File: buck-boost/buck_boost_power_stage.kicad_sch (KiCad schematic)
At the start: 21 parts, among them K1 Relay_SPDT, K2 Relay_SPDT, Q1 Q_NMOS_GDS, Q2 Q_NMOS_GDS, Q3 Q_NMOS_GDS, Q4 Q_NMOS_GDS, Q5 Q_NMOS_GDS

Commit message: Updating schematics notes
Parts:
- removed C15, C17: TBD, symbol Device:C_Polarized
- C14, C16: footprint (none) -> CL_Capacitor_PTH:C_Rect_L43.0mm_W36.0mm_P37.50_27.50_22.50mm_S20.3_10.2mm_Film
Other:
- note added: "Notes [1] V_s1 and V_s3 are the source voltages of Q1 and Q3. These nodes are used as reference for their gate drivers. [2] Two of these are bulk electrolytic capacitors, and one is low-esr (lower capacitance) capacitors."
- note removed: "Ceramic or film caps?"
- note removed: "Notes [1] V_s1 and V_s3 are the source voltages of Q1 and Q3. These nodes are used as reference for their gate drivers. [2] Two of these are bulk electrolytic capacitors, and two are low-esr (lower capacitance) capacitors."
- moved on the sheet: C14, C8, C9, K1, K2, Q5, R6

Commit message: Working on gate drivers of buck boost platform
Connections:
- net S1 renamed G_S1
- net S2 renamed G_S2
- net S3 renamed G_S3
- net S4 renamed G_S4
- net S_load renamed G_Sload
- net V_s1 renamed Vs_S1
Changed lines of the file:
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@@
 		)
 	)
-	(label "S_load"
+	(label "G_Sload"
 		(at 229.87 52.07 180)
 		(fields_autoplaced yes)
@@
 		)
 	)
-	(label "V_s3"
+	(label "Vs_S3"
 		(at 67.31 83.82 0)
 		(fields_autoplaced yes)
@@
 		)
 	)
-	(label "S1"
+	(label "G_S1"
 		(at 67.31 76.2 0)
 		(fields_autoplaced yes)
@@
 		)
 	)
-	(label "S2"
+	(label "G_S2"
 		(at 92.71 76.2 0)
 		(fields_autoplaced yes)
@@
 		)
 	)
-	(label "S1"
+	(label "G_S1"
 		(at 105.41 36.83 180)
 		(fields_autoplaced yes)
@@
 		)
 	)
-	(label "V_s1"
+	(label "Vs_S1"
 		(at 67.31 78.74 0)
 		(fields_autoplaced yes)
@@
 		)
 	)
-	(label "V_s3"
+	(label "Vs_S3"
 		(at 143.51 44.45 0)
 		(fields_autoplaced yes)
@@
 		)
 	)
-	(label "S3"
+	(label "G_S3"
 		(at 67.31 81.28 0)
 		(fields_autoplaced yes)
@@
 		)
 	)
-	(label "S3"
+	(label "G_S3"
 		(at 151.13 36.83 0)
 		(fields_autoplaced yes)
@@
 		)
 	)
-	(label "V_s1"
+	(label "Vs_S1"
 		(at 113.03 44.45 180)
 		(fields_autoplaced yes)
@@
 		)
 	)
-	(label "S4"
+	(label "G_S4"
 		(at 151.13 52.07 0)
 		(fields_autoplaced yes)
@@
 		)
 	)
-	(label "S_load"
+	(label "G_Sload"
 		(at 92.71 81.28 0)
 		(fields_autoplaced yes)
@@
 		)
 	)
-	(label "S4"
+	(label "G_S4"
 		(at 92.71 78.74 0)
 		(fields_autoplaced yes)
@@
 		)
 	)
-	(label "S2"
+	(label "G_S2"
 		(at 105.41 52.07 180)
 		(fields_autoplaced yes)
@@
 		)
 	)
-	(hierarchical_label "V_s3"
+	(hierarchical_label "Vs_S3"
 		(shape bidirectional)
 		(at 73.66 83.82 0)
@@
 		)
 	)
-	(hierarchical_label "S4"
+	(hierarchical_label "G_S4"
 		(shape bidirectional)
 		(at 101.6 78.74 0)
@@
 		)
 	)
-	(hierarchical_label "V_s1"
+	(hierarchical_label "Vs_S1"
 		(shape bidirectional)
 		(at 73.66 78.74 0)
@@
 		)
 	)
-	(hierarchical_label "S3"
+	(hierarchical_label "G_S3"
 		(shape bidirectional)
 		(at 73.66 81.28 0)
@@
 		)
 	)
-	(hierarchical_label "S1"
+	(hierarchical_label "G_S1"
 		(shape bidirectional)
 		(at 73.66 76.2 0)
@@
 		)
 	)
-	(hierarchical_label "S2"
+	(hierarchical_label "G_S2"
 		(shape bidirectional)
 		(at 101.6 76.2 0)
@@
 		)
 	)
-	(hierarchical_label "S_load"
+	(hierarchical_label "G_Sload"
 		(shape bidirectional)
 		(at 101.6 81.28 0)

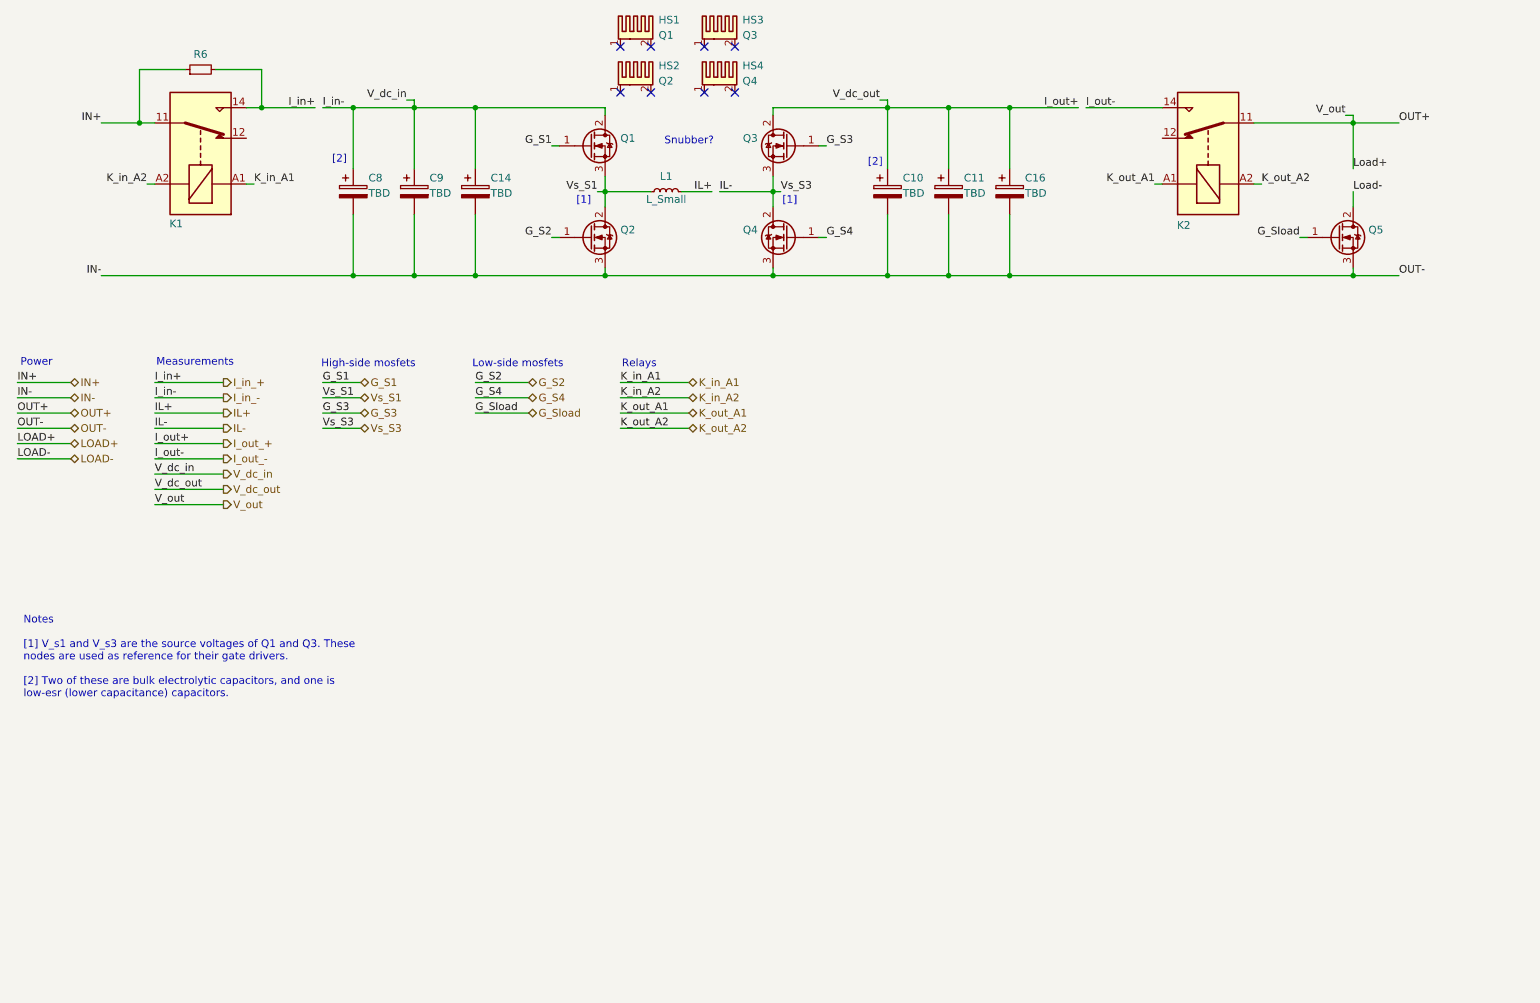
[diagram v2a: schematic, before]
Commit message: Added load switch and relay drivers
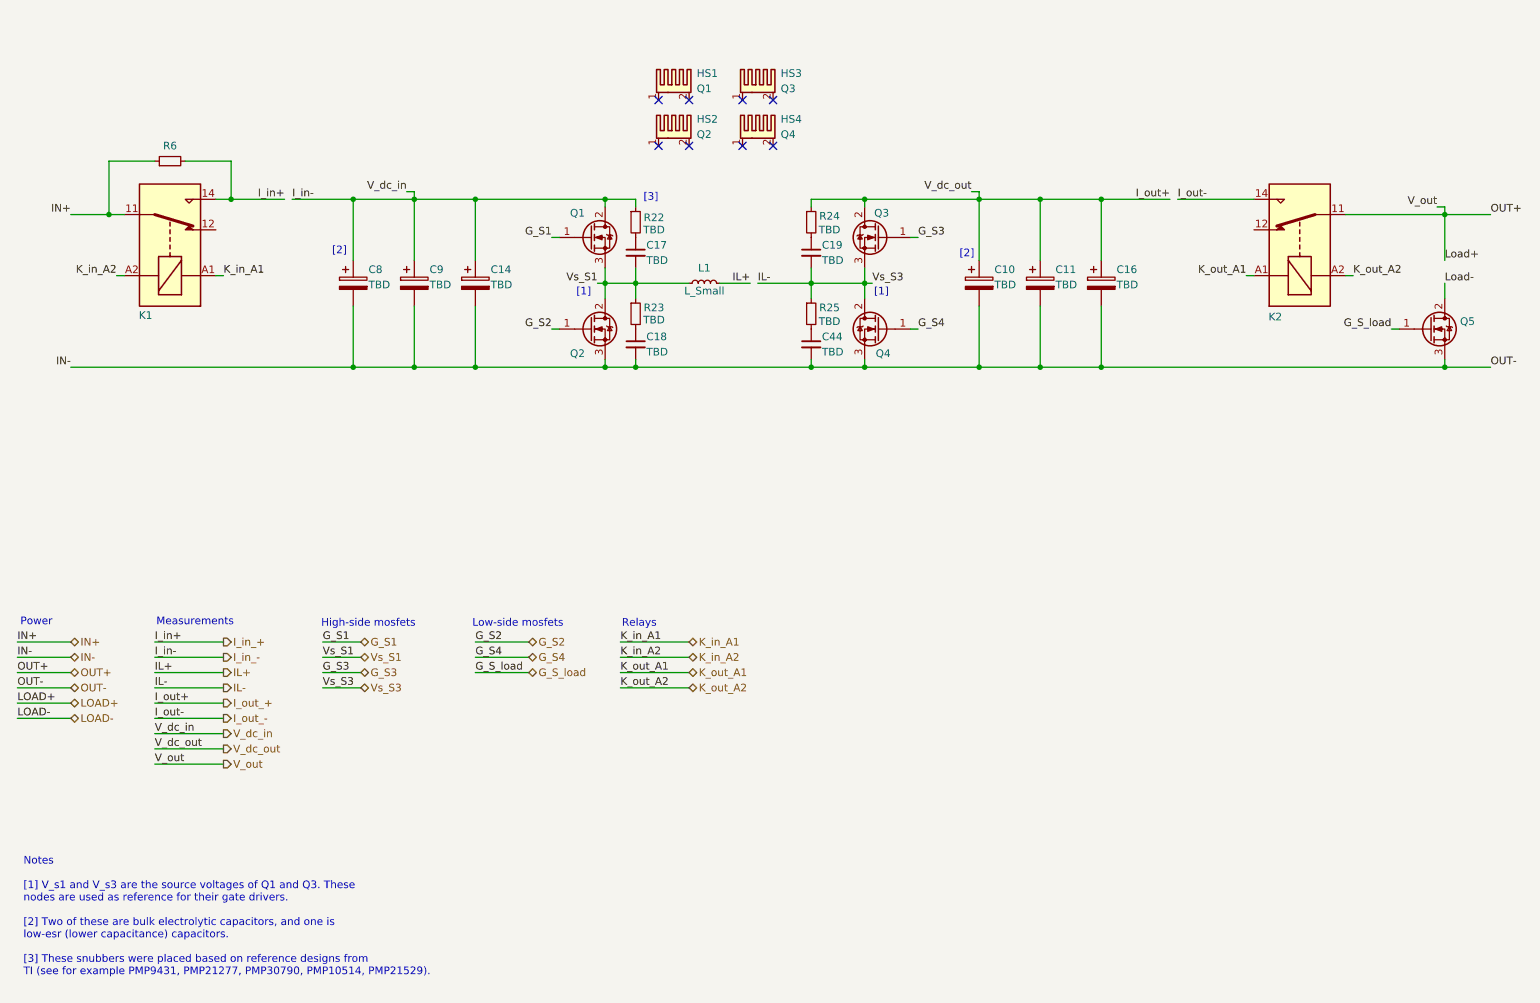
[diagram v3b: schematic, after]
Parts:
- added C17, C18, C19, C44: TBD, Capacitor_SMD:C_0805_2012Metric_Pad1.18x1.45mm_HandSolder, symbol Device:C_Small
- added R22, R23, R24, R25: TBD, symbol Device:R_Small
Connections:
- net IL-: now also C19.2, R25.1
- net IN-: now also C18.2, C44.2
- net I_in_-: now also R22.1
- net I_out_+: now also R24.1
- net Vs_S1: now also C17.2, R23.1
- net G_Sload renamed G_S_load
- new net: C19.1, R24.2
- new net: C17.1, R22.2
- new net: C44.1, R25.2
- new net: C18.1, R23.2
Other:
- note added: "Notes [1] V_s1 and V_s3 are the source voltages of Q1 and Q3. These nodes are used as reference for their gate drivers. [2] Two of these are bulk electrolytic capacitors, and one is low-esr (lower capacitance) capacitors. [3] These snubbers were placed based on reference designs from TI (see for example PMP9431, PMP21277, PMP30790, PMP10514, PMP21529)."
- note added: "[3]"
- note removed: "Notes [1] V_s1 and V_s3 are the source voltages of Q1 and Q3. These nodes are used as reference for their gate drivers. [2] Two of these are bulk electrolytic capacitors, and one is low-esr (lower capacitance) capacitors."
- note removed: "Snubber?"
- moved on the sheet: C10, C11, C14, C16, C8, C9, HS1, HS2, HS3, HS4, K1, K2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

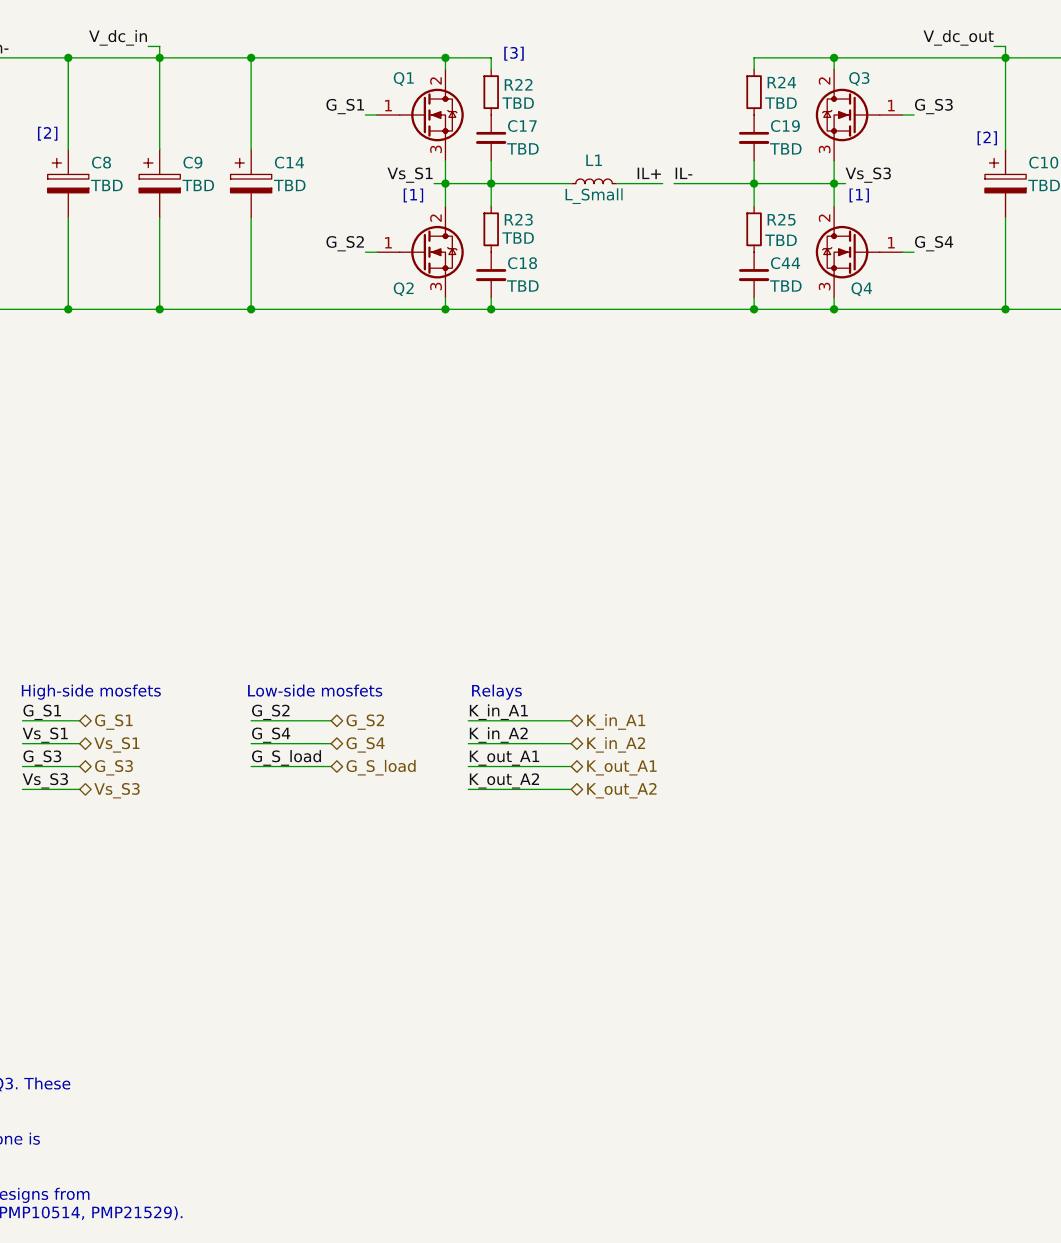
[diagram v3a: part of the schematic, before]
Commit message: Adding current and voltage measurements blocks
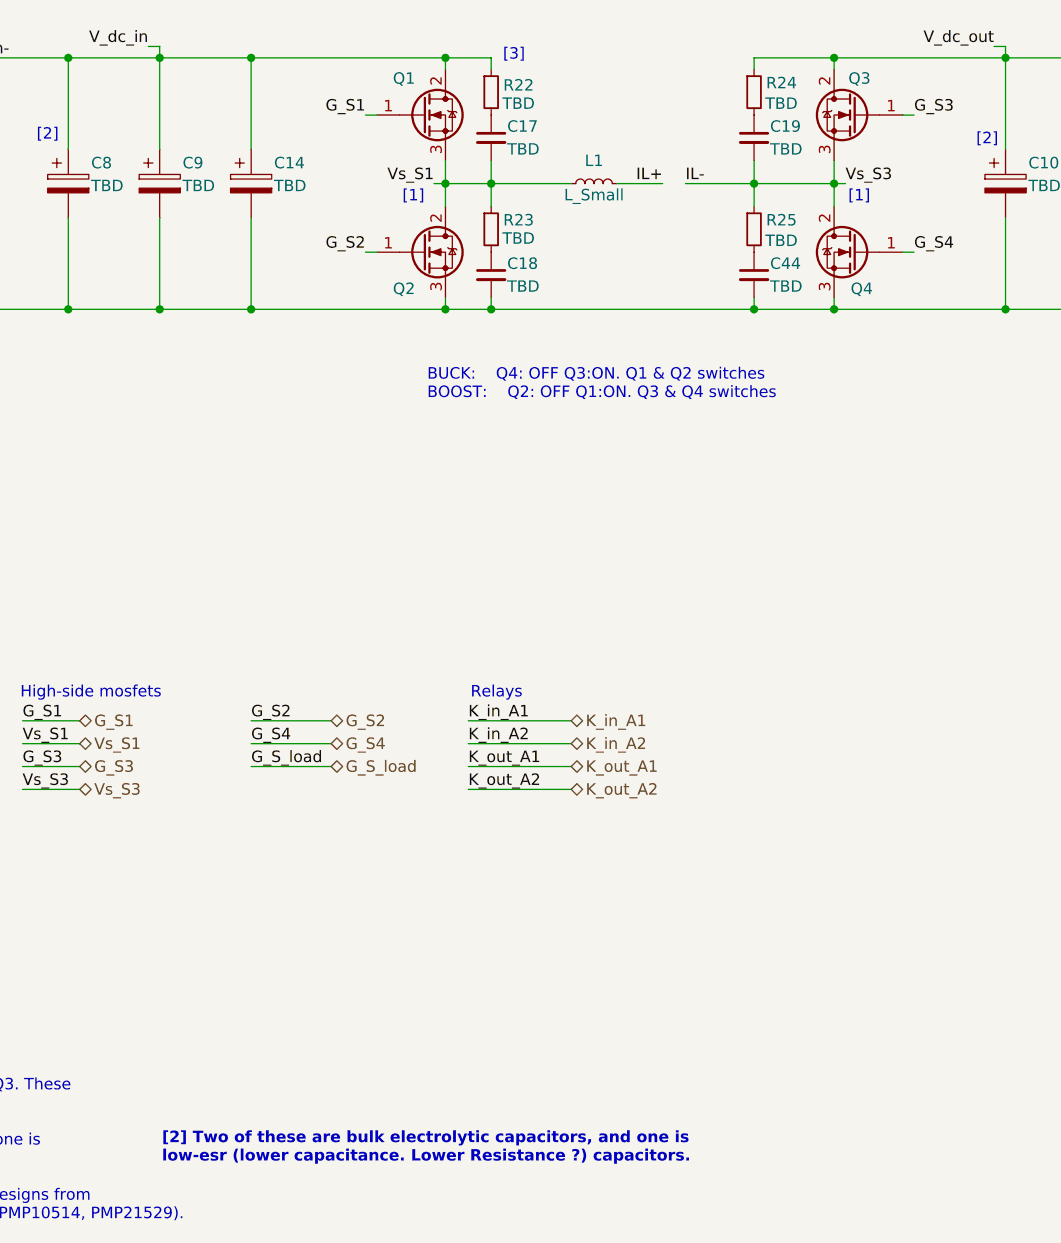
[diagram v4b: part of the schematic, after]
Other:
- note added: "BUCK: Q4: OFF Q3:ON. Q1 & Q2 switches BOOST: Q2: OFF Q1:ON. Q3 & Q4 switches"
- note added: "[2] Two of these are bulk electrolytic capacitors, and one is low-esr (lower capacitance. Lower Resistance ?) capacitors."
- note removed: "Low-side mosfets"
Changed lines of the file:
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@@
-	(wire
-		(pts
-			(xy 139.7 59.69) (xy 148.59 59.69)
-		)
-		(stroke
-			(width 0)
-			(type default)
-		)
-	)
 	(wire
 		(pts
@@
 	(wire
 		(pts
-			(xy 133.35 59.69) (xy 138.43 59.69)
-		)
-		(stroke
-			(width 0)
-			(type default)
-		)
-	)
-	(wire
-		(pts
 			(xy 92.71 124.46) (xy 101.6 124.46)
 		)
@@
 	(wire
 		(pts
+			(xy 140.97 59.69) (xy 148.59 59.69)
+		)
+		(stroke
+			(width 0)
+			(type default)
+		)
+	)
+	(wire
+		(pts
 			(xy 254 55.88) (xy 254 48.26)
 		)
@@
 	(wire
 		(pts
+			(xy 148.59 57.15) (xy 148.59 59.69)
+		)
+		(stroke
+			(width 0)
+			(type default)
+		)
+	)
+	(wire
+		(pts
 			(xy 148.59 45.72) (xy 157.48 45.72)
 		)
@@
 	(wire
 		(pts
-			(xy 148.59 57.15) (xy 148.59 59.69)
-		)
-		(stroke
-			(width 0)
-			(type default)
-		)
-	)
-	(wire
-		(pts
 			(xy 44.45 39.37) (xy 52.07 39.37)
 		)
@@
 		(pts
 			(xy 196.85 45.72) (xy 196.85 55.88)
+		)
+		(stroke
+			(width 0)
+			(type default)
+		)
+	)
+	(wire
+		(pts
+			(xy 138.43 59.69) (xy 133.35 59.69)
 		)
 		(stroke
@@
 		)
 	)
-	(text "Low-side mosfets"
+	(text "BUCK:	Q4: OFF Q3:ON. Q1 & Q2 switches\nBOOST:	Q2: OFF Q1:ON. Q3 & Q4 switches\n"
 		(exclude_from_sim no)
-		(at 92.202 116.332 0)
+		(at 112.268 82.042 0)
 		(effects
 			(font
@@
 		)
 	)
+	(text "[2] Two of these are bulk electrolytic capacitors, and one is\nlow-esr (lower capacitance. Lower Resistance ?) capacitors."
+		(exclude_from_sim no)
+		(at 82.804 166.878 0)
+		(effects
+			(font
+				(size 1.27 1.27)
+				(thickness 0.254)
+				(bold yes)
+				(color 255 0 13 1)
+			)
+			(justify left)
+		)
+	)
 	(text "High-side mosfets"
 		(exclude_from_sim no)
@@
 	)
 	(label "IL-"
-		(at 139.7 59.69 0)
-		(fields_autoplaced yes)
-		(effects
+		(at 140.97 59.69 0)
+		(fields_autoplaced yes)
+		(effects
